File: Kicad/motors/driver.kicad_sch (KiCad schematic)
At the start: 38 parts

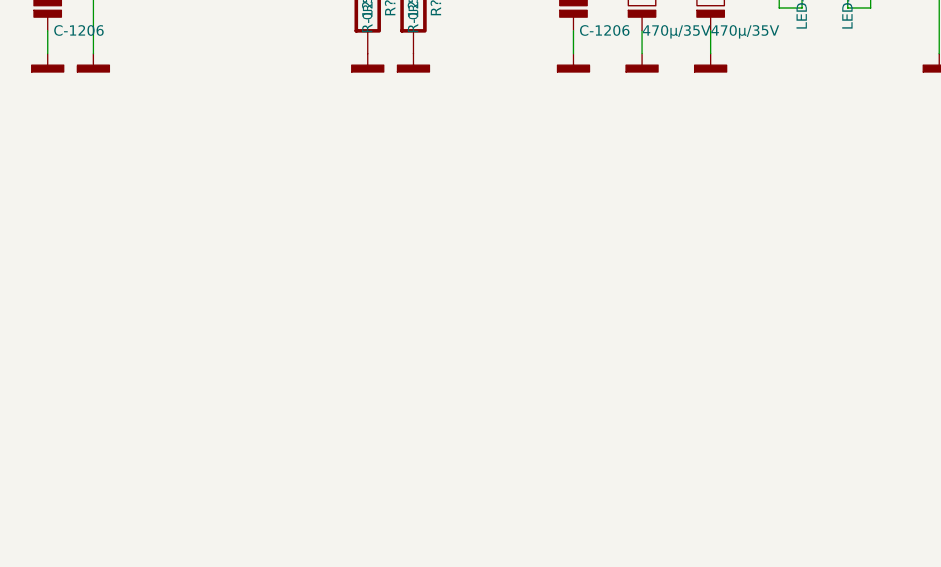
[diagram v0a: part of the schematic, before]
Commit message: Update Motors
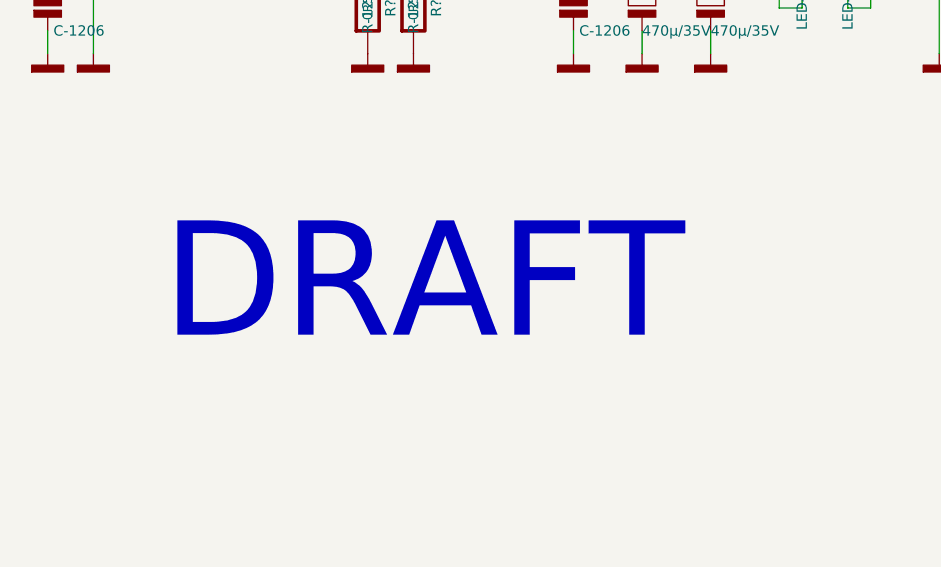
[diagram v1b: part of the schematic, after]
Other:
- note added: "DRAFT"
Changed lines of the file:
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@@
     (effects (font (size 1.27 1.27)) (justify right bottom))
+  )
+  (text "DRAFT" (at 114.3 116.84 0)
+    (effects (font (size 12.7 12.7)) (justify left bottom))
   )
   (text "M1-\n" (at 243.84 49.53 180)

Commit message: Update Motor
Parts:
- removed TP?: KEYSTONE-5006, tronixio:KEYSTONE-5006, symbol tronixio:KEYSTONE-5006
- added TP?: HARWIN-S1751, tronixio:zzzHARWIN-S1751, symbol tronixio:HARWIN-S1751
- C?: value C-1206 -> 100n
- C? (x2): value C-1206 -> 1µ; Name 1µ -> (none)
- C? (x3): value C-1206 -> 100n; Name 100n -> (none)
- IC? (x2): value SN74LVC1G19-SOT -> SN74LVC1G19; Name SN74LVC1G19 -> (none)
- IC? (x4): Name SN74LVC1G19 -> (none)
- IC?: value LM3480-50-SOT -> LM3480-50; Name LM3480-50 -> (none)
- IC?: Name L298P -> (none)
- LED? (x4): value LED-1206-ORANGE -> Red; symbol tronixio:LED-1206-ORANGE -> tronixio:LED-1206-RED; MOUSER 604-APT3216LSECKJ4RV -> 604-APT3216LSECKJ3RV
- LED?: value LED-1206-ORANGE -> +5V; symbol tronixio:LED-1206-ORANGE -> tronixio:LED-1206-RED; MOUSER 604-APT3216LSECKJ4RV -> 604-APT3216LSECKJ3RV
- R? (x3): value R-1206 -> 10K; Name 10K -> (none)
- R? (x2): value R-1210 -> 0Ω5; Name 0R5 -> (none)
- R?: value R-1206 -> 12K; Name 12K -> (none)
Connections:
- net +5V: now also TP?.1
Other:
- title: Motor Driver -> Motors Driver

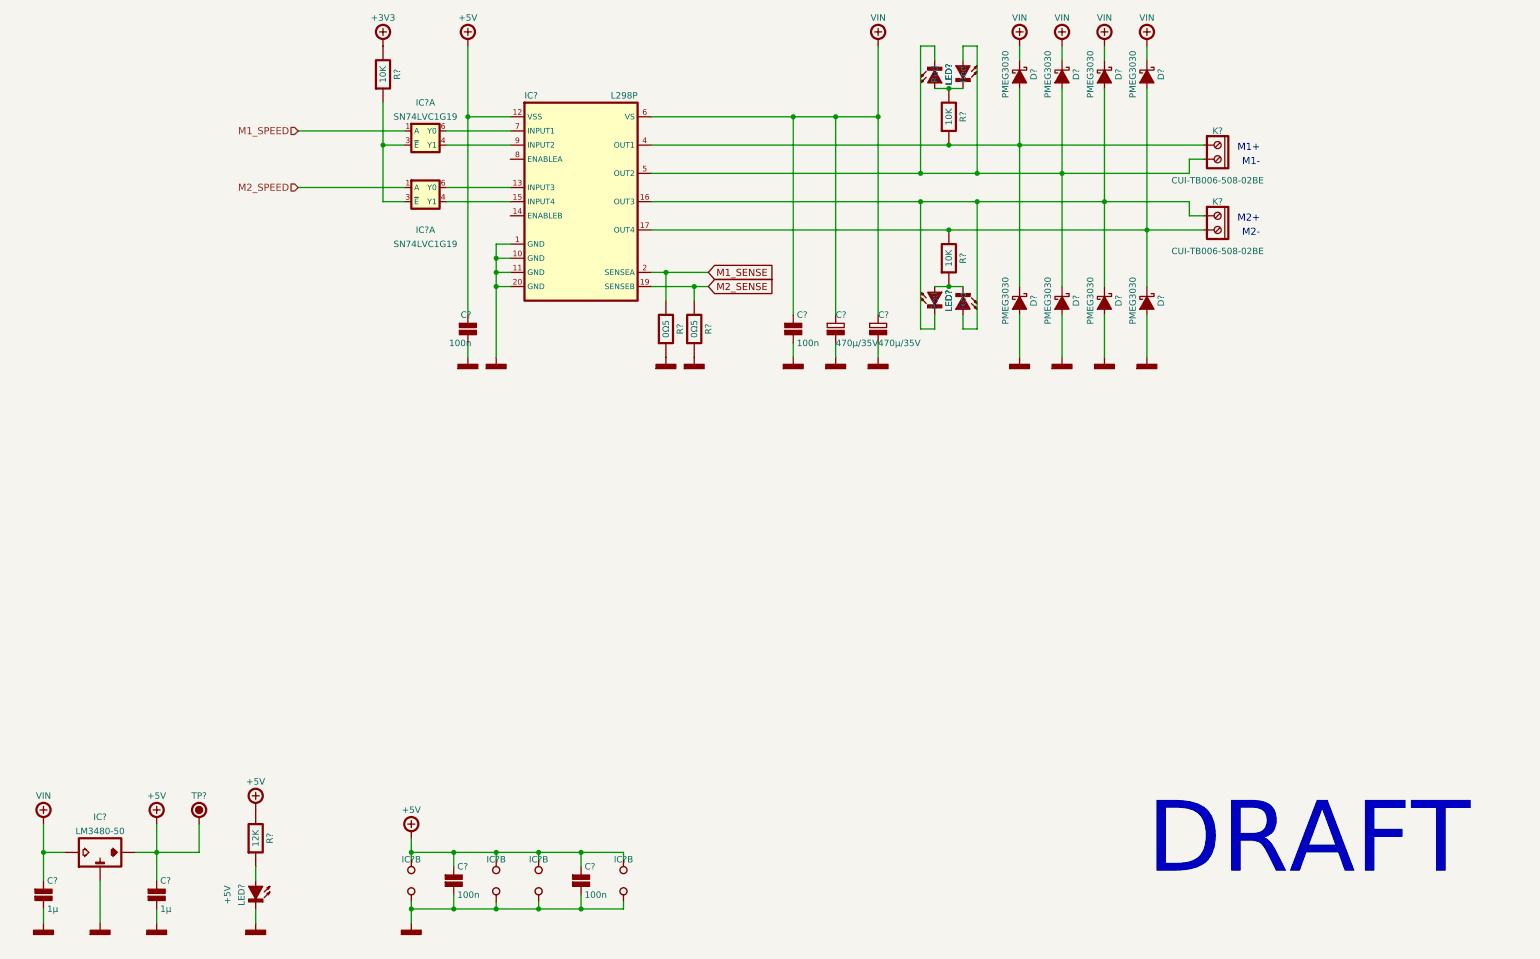
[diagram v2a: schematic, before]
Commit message: Update Motors
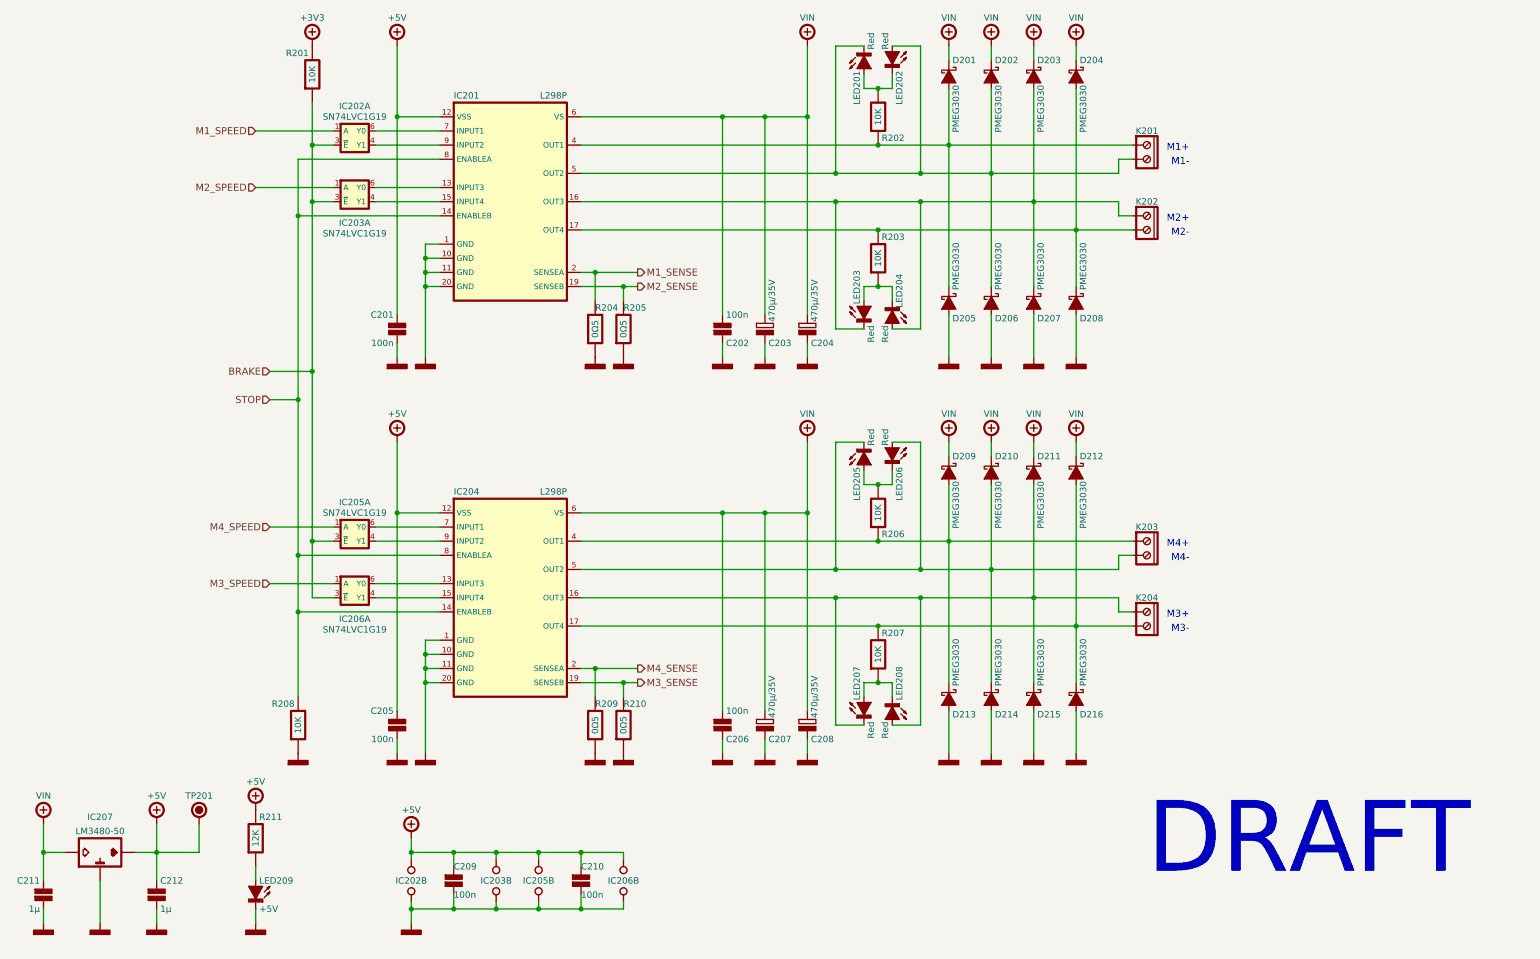
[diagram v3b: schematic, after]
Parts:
- removed IC? (x4): SN74LVC1G19-SOT, tronixio:SOT-23-6, symbol tronixio:SN74LVC1G19-SOT
- added C205, C206: 100n, tronixio:CAPACITOR-1206, symbol tronixio:C-1206
- added C207, C208: UVZ-470U-35V, tronixio:CAPACITOR-ELECTROLYTIC-RADIAL-100-160-050, symbol tronixio:UVZ-470U-35V
- added D209, D210, D211, D212, D213, D214, D215, D216: PMEG3030, tronixio:SOD-128, symbol tronixio:PMEG3030
- added unit 2 of IC202
- added unit 2 of IC203
- added IC204: L298P, tronixio:zzzSOPOWER-20, symbol tronixio:L298P
- added IC205, IC206: SN74LVC1G19, tronixio:SOT-23-6, symbol tronixio:SN74LVC1G19-SOT
- added K203: MOTOR 4, tronixio:CUI-TB006-508-02BE, symbol tronixio:CUI-TB006-508-02BE
- added K204: MOTOR 3, tronixio:CUI-TB006-508-02BE, symbol tronixio:CUI-TB006-508-02BE
- added LED205, LED206, LED207, LED208: Red, tronixio:LED-1206, symbol tronixio:LED-1206-RED
- added R206, R207: 10K, tronixio:RESISTOR-1206, symbol tronixio:R-1206
- added R208: 10K, tronixio:RESISTOR-1210, symbol tronixio:R-1210
- added R209, R210: 0Ω5, tronixio:RESISTOR-1210, symbol tronixio:R-1210
- IC201: renamed from IC?; footprint tronixio:SOPOWER-20 -> tronixio:zzzSOPOWER-20
- K201: renamed from K?; value CUI-TB006-508-02BE -> MOTOR 1
- K202: renamed from K?; value CUI-TB006-508-02BE -> MOTOR 2
- gave numbers to parts that had none: 31
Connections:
- net +5V: now also C205.1, IC202.5 (VCC), IC203.5 (VCC), IC204.12 (VSS), IC205.5 (VCC), IC206.5 (VCC)
- net GND: now also C205.2, C206.2, C207.2, C208.2, D213.2 (A), D214.2 (A), D215.2 (A), D216.2 (A), IC202.2 (GND), IC203.2 (GND), IC204.1 (GND), IC204.10 (GND), IC204.11 (GND), IC204.20 (GND), IC205.2 (GND), IC206.2 (GND), R208.2, R209.2, R210.2
- net VIN: now also C206.1, C207.1, C208.1, D209.1 (C), D210.1 (C), D211.1 (C), D212.1 (C), IC204.6 (VS)
- net BRAKE: now reaches IC202.3 (~{E}), IC203.3 (~{E}), R201.2
- net BRAKE: now also IC205.3 (~{E}), IC206.3 (~{E})
- net STOP: now reaches IC201.14 (ENABLEB)
- net STOP: now also IC201.8 (ENABLEA), IC204.14 (ENABLEB), IC204.8 (ENABLEA), R208.1
- new net: D212.2 (A), D216.1 (C), IC204.17 (OUT4), K204.2, R207.1
- new net: D209.2 (A), D213.1 (C), IC204.4 (OUT1), K203.1, R206.2
- new net: D211.2 (A), D215.1 (C), IC204.16 (OUT3), K204.1, LED207.1 (K), LED208.2 (A)
- new net: LED205.2 (A), LED206.1 (K), R206.1
- new net: D210.2 (A), D214.1 (C), IC204.5 (OUT2), K203.2, LED205.1 (K), LED206.2 (A)
- new net: IC204.9 (INPUT2), IC205.4 (Y1)
- new net: IC204.7 (INPUT1), IC205.6 (Y0)
- new net: IC204.15 (INPUT4), IC206.4 (Y1)
- new net: IC204.13 (INPUT3), IC206.6 (Y0)
- new net: LED207.2 (A), LED208.1 (K), R207.2
- new net M3_SENSE: IC204.19 (SENSEB), R210.1
- new net M3_SPEED: IC206.1 (A)
- new net M4_SENSE: IC204.2 (SENSEA), R209.1
- new net M4_SPEED: IC205.1 (A)
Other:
- note added: "M3+"
- note added: "M3-"
- note added: "M4+"
- note added: "M4-"
- moved on the sheet: C201, C202, C203, C204, D201, D202, D203, D204, D205, D206, D207, D208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

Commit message: Update Motor
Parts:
- C203, C204, C207, C208: footprint tronixio:CAPACITOR-ELECTROLYTIC-RADIAL-100-160-050 -> tronixio:zzzCAPACITOR-ELECTROLYTIC-RADIAL-100-160-050
- R208: footprint tronixio:RESISTOR-1210 -> tronixio:RESISTOR-1206
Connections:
- net GND: now also IC201.21 (PAD_GND), IC204.21 (PAD_GND)
- net M3-: now reaches D212.2 (A), D216.1 (C), IC204.17 (OUT4), K204.2, R207.1
- net M2+: now reaches D203.2 (A), D207.1 (C), IC201.16 (OUT3), K202.1, LED203.1 (K), LED204.2 (A)
- net M1-: now reaches D202.2 (A), D206.1 (C), IC201.5 (OUT2), LED201.1 (K), LED202.2 (A)
- net M1-: now also K201.1; no longer K201.2
- net M4+: now reaches D209.2 (A), D213.1 (C), IC204.4 (OUT1), R206.2
- net M4+: now also K203.2; no longer K203.1
- net M3+: now reaches D211.2 (A), D215.1 (C), IC204.16 (OUT3), K204.1, LED207.1 (K), LED208.2 (A)
- net M4-: now reaches D210.2 (A), D214.1 (C), IC204.5 (OUT2), LED205.1 (K), LED206.2 (A)
- net M4-: now also K203.1; no longer K203.2
- net M2-: now reaches D204.2 (A), D208.1 (C), IC201.17 (OUT4), K202.2, R203.1
- net M1+: now reaches D201.2 (A), D205.1 (C), IC201.4 (OUT1), R202.2
- net M1+: now also K201.2; no longer K201.1
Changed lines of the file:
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@@
   (junction (at 129.54 142.24) (diameter 0.9144) (color 0 0 0 0)
   )
+  (junction (at 93.98 63.5) (diameter 0) (color 0 0 0 0)
+  )
   (junction (at 93.98 139.7) (diameter 0.9144) (color 0 0 0 0)
   )
@@
   (junction (at 203.2 55.88) (diameter 0.9144) (color 0 0 0 0)
   )
+  (junction (at 93.98 134.62) (diameter 0) (color 0 0 0 0)
+  )
   (junction (at 91.44 172.72) (diameter 0.9144) (color 0 0 0 0)
   )
@@
     (stroke (width 0) (type solid) (color 0 0 0 0))
   )
+  (wire (pts (xy 96.52 132.08) (xy 93.98 132.08))
+    (stroke (width 0) (type default) (color 0 0 0 0))
+  )
   (wire (pts (xy 93.98 137.16) (xy 96.52 137.16))
     (stroke (width 0) (type solid) (color 0 0 0 0))
@@
     (stroke (width 0) (type solid) (color 0 0 0 0))
   )
+  (wire (pts (xy 93.98 132.08) (xy 93.98 134.62))
+    (stroke (width 0) (type default) (color 0 0 0 0))
+  )
   (wire (pts (xy 35.56 177.8) (xy 35.56 185.42))
     (stroke (width 0) (type solid) (color 0 0 0 0))
@@
     (stroke (width 0) (type solid) (color 0 0 0 0))
   )
+  (wire (pts (xy 96.52 60.96) (xy 93.98 60.96))
+    (stroke (width 0) (type default) (color 0 0 0 0))
+  )
   (wire (pts (xy 93.98 142.24) (xy 96.52 142.24))
     (stroke (width 0) (type solid) (color 0 0 0 0))
@@
   )
   (wire (pts (xy 182.88 127) (xy 182.88 149.86))
+    (stroke (width 0) (type default) (color 0 0 0 0))
+  )
+  (wire (pts (xy 93.98 60.96) (xy 93.98 63.5))
     (stroke (width 0) (type default) (color 0 0 0 0))
   )
@@
     (effects (font (size 1.27 1.27)) (justify right bottom))
   )
-  (text "DRAFT" (at 223.52 177.8 0)
-    (effects (font (size 12.7 12.7)) (justify left bottom))
+  (text "DRAFT" (at 213.36 187.96 0)
+    (effects (font (size 4 4)) (justify left bottom))
   )
   (text "M3+" (at 231.14 130.81 180)
@@
     (effects (font (size 1.27 1.27)) (justify right bottom))
   )
+  (label "M4-" (at 121.92 121.92 0)
+    (effects (font (size 1.27 1.27)) (justify left bottom))
+  )
+  (label "M1-" (at 121.92 50.8 0)
+    (effects (font (size 1.27 1.27)) (justify left bottom))
+  )
+  (label "M1+" (at 121.92 45.72 0)
+    (effects (font (size 1.27 1.27)) (justify left bottom))
+  )
+  (label "M3+" (at 121.92 127 0)
+    (effects (font (size 1.27 1.27)) (justify left bottom))
+  )
+  (label "M2+" (at 121.92 55.88 0)
+    (effects (font (size 1.27 1.27)) (justify left bottom))
+  )
+  (label "M3-" (at 121.92 132.08 0)
+    (effects (font (size 1.27 1.27)) (justify left bottom))
+  )
+  (label "M2-" (at 121.92 60.96 0)
+    (effects (font (size 1.27 1.27)) (justify left bottom))
+  )
+  (label "M4+" (at 121.92 116.84 0)
+    (effects (font (size 1.27 1.27)) (justify left bottom))
+  )
   (hierarchical_label "M4_SENSE" (shape output) (at 132.08 139.7 0)
     (effects (font (size 1.27 1.27)) (justify left))
@@
       (effects (font (size 1 1)) hide)
     )
-    (property "Footprint" "tronixio:CAPACITOR-ELECTROLYTIC-RADIAL-100-160-050" (id 2) (at 154.94 162.56 0)
+    (property "Footprint" "tronixio:zzzCAPACITOR-ELECTROLYTIC-RADIAL-100-160-050" (id 2) (at 154.94 162.56 0)
       (effects (font (size 1 1)) hide)
     )
@@
   (symbol (lib_id "tronixio:LED-1206-RED") (at 177.8 76.2 270) (unit 1)
     (in_bom yes) (on_board yes)
-    (property "Reference" "LED204" (id 0) (at 179.07 74.93 0)
+    (property "Reference" "LED204" (id 0) (at 179.07 74.295 0)
       (effects (font (size 1.15 1.15)) (justify right))
     )
@@
       (effects (font (size 1.15 1.15)))
     )
-    (property "Footprint" "tronixio:RESISTOR-1210" (id 2) (at 71.12 162.56 0)
+    (property "Footprint" "tronixio:RESISTOR-1206" (id 2) (at 71.12 162.56 0)
       (effects (font (size 1 1)) hide)
     )
@@
       (effects (font (size 1 1)) hide)
     )
-    (property "Footprint" "tronixio:CAPACITOR-ELECTROLYTIC-RADIAL-100-160-050" (id 2) (at 162.56 91.44 0)
+    (property "Footprint" "tronixio:zzzCAPACITOR-ELECTROLYTIC-RADIAL-100-160-050" (id 2) (at 162.56 91.44 0)
       (effects (font (size 1 1)) hide)
     )
@@
     (pin "2")
   )
-  (symbol (lib_id "tronixio:CUI-TB006-508-02BE") (at 223.52 116.84 0) (unit 1)
-    (in_bom yes) (on_board yes)
-    (property "Reference" "K203" (id 0) (at 223.52 114.3 0)
-      (effects (font (size 1.15 1.15)))
-    )
-    (property "Value" "MOTOR 4" (id 1) (at 223.52 123.19 0)
+  (symbol (lib_id "tronixio:CUI-TB006-508-02BE") (at 223.52 119.38 0) (mirror x) (unit 1)
+    (in_bom yes) (on_board yes)
+    (property "Reference" "K203" (id 0) (at 223.52 121.92 0)
+      (effects (font (size 1.15 1.15)))
+    )
+    (property "Value" "MOTOR 4" (id 1) (at 223.52 113.03 0)
       (effects (font (size 1.15 1.15)) hide)
     )
-    (property "Footprint" "tronixio:CUI-TB006-508-02BE" (id 2) (at 223.52 127 0)
-      (effects (font (size 1 1)) hide)
-    )
-    (property "Datasheet" "https://www.cuidevices.com/product/interconnect/connectors/terminal-blocks/tb006-508-series" (id 3) (at 223.52 129.54 0)
-      (effects (font (size 1 1)) hide)
-    )
-    (property "MOUSER" "490-TB006-508-02BE" (id 4) (at 223.52 132.08 0)
+    (property "Footprint" "tronixio:CUI-TB006-508-02BE" (id 2) (at 223.52 109.22 0)
+      (effects (font (size 1 1)) hide)
+    )
+    (property "Datasheet" "https://www.cuidevices.com/product/interconnect/connectors/terminal-blocks/tb006-508-series" (id 3) (at 223.52 106.68 0)
+      (effects (font (size 1 1)) hide)
+    )
+    (property "MOUSER" "490-TB006-508-02BE" (id 4) (at 223.52 104.14 0)
       (effects (font (size 1 1)) hide)
     )
@@
       (effects (font (size 1 1)) hide)
     )
-    (property "Footprint" "tronixio:CAPACITOR-ELECTROLYTIC-RADIAL-100-160-050" (id 2) (at 162.56 162.56 0)
+    (property "Footprint" "tronixio:zzzCAPACITOR-ELECTROLYTIC-RADIAL-100-160-050" (id 2) (at 162.56 162.56 0)
       (effects (font (size 1 1)) hide)
     )
@@
     (pin "16")
     (pin "17")
+    (pin "18")
     (pin "19")
     (pin "2")
     (pin "20")
+    (pin "21")
+    (pin "3")
     (pin "4")
     (pin "5")
@@
       (effects (font (size 1 1)) hide)
     )
-    (property "Footprint" "tronixio:CAPACITOR-ELECTROLYTIC-RADIAL-100-160-050" (id 2) (at 154.94 91.44 0)
+    (property "Footprint" "tronixio:zzzCAPACITOR-ELECTROLYTIC-RADIAL-100-160-050" (id 2) (at 154.94 91.44 0)
       (effects (font (size 1 1)) hide)
     )
@@
     (pin "1")
   )
-  (symbol (lib_id "tronixio:CUI-TB006-508-02BE") (at 223.52 45.72 0) (unit 1)
-    (in_bom yes) (on_board yes)
-    (property "Reference" "K201" (id 0) (at 223.52 43.18 0)
-      (effects (font (size 1.15 1.15)))
-    )
-    (property "Value" "MOTOR 1" (id 1) (at 223.52 52.07 0)
+  (symbol (lib_id "tronixio:CUI-TB006-508-02BE") (at 223.52 48.26 0) (mirror x) (unit 1)
+    (in_bom yes) (on_board yes)
+    (property "Reference" "K201" (id 0) (at 223.52 50.8 0)
+      (effects (font (size 1.15 1.15)))
+    )
+    (property "Value" "MOTOR 1" (id 1) (at 223.52 41.91 0)
       (effects (font (size 1.15 1.15)) hide)
     )
-    (property "Footprint" "tronixio:CUI-TB006-508-02BE" (id 2) (at 223.52 55.88 0)
-      (effects (font (size 1 1)) hide)
-    )
-    (property "Datasheet" "https://www.cuidevices.com/product/interconnect/connectors/terminal-blocks/tb006-508-series" (id 3) (at 223.52 58.42 0)
-      (effects (font (size 1 1)) hide)
-    )
-    (property "MOUSER" "490-TB006-508-02BE" (id 4) (at 223.52 60.96 0)
+    (property "Footprint" "tronixio:CUI-TB006-508-02BE" (id 2) (at 223.52 38.1 0)
+      (effects (font (size 1 1)) hide)
+    )
+    (property "Datasheet" "https://www.cuidevices.com/product/interconnect/connectors/terminal-blocks/tb006-508-series" (id 3) (at 223.52 35.56 0)
+      (effects (font (size 1 1)) hide)
+    )
+    (property "MOUSER" "490-TB006-508-02BE" (id 4) (at 223.52 33.02 0)
       (effects (font (size 1 1)) hide)
     )
@@
     (pin "16")
     (pin "17")
+    (pin "18")
     (pin "19")
     (pin "2")
     (pin "20")
+    (pin "21")
+    (pin "3")
     (pin "4")
     (pin "5")
